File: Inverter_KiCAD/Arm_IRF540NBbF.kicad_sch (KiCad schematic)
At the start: 23 parts, among them Q10 HCPL-315J-500E, Q2 IRF540N, Q3 IRF540N, U1 MPRB2415S-6W, U15 HCPL-7800A, U4 MPRB2415S-6W, U6 GO 10-SME/SP3

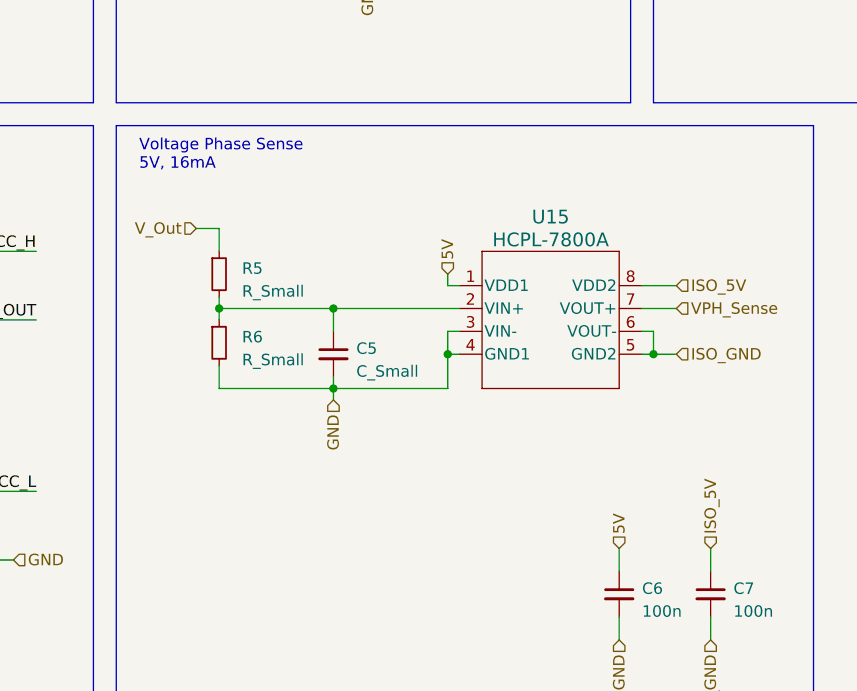
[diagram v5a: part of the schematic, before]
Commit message: start schematic Nucleo board
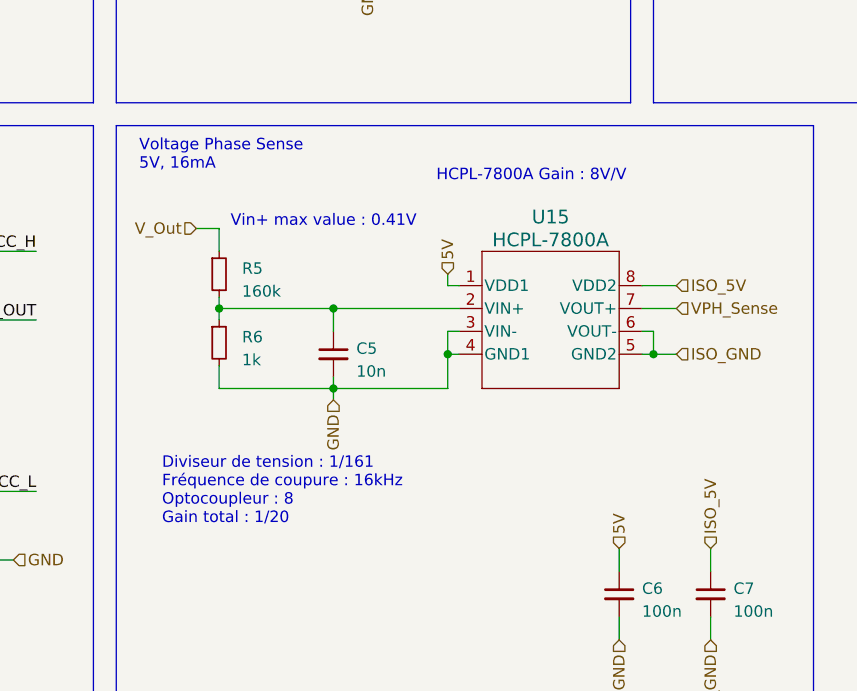
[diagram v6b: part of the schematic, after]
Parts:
- C5: value C_Small -> 10n
- R5: value R_Small -> 160k
- R6: value R_Small -> 1k
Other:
- note added: "Diviseur de tension : 1/161 Fréquence de coupure : 16kHz Optocoupleur : 8 Gain total : 1/20"
- note added: "HCPL-7800A Gain : 8V/V"
- note added: "Vin+ max value : 0.41V"
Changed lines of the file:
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@@
+    (effects (font (size 1.27 1.27)) (justify left bottom))
+  )
+  (text "Vin+ max value : 0.41V" (at 127 96.52 0)
     (effects (font (size 1.27 1.27)) (justify left bottom))
   )
@@
     (effects (font (size 1.27 1.27)) (justify left bottom))
   )
+  (text "Diviseur de tension : 1/161\nFréquence de coupure : 16kHz\nOptocoupleur : 8\nGain total : 1/20"
+    (at 119.38 129.54 0)
+    (effects (font (size 1.27 1.27)) (justify left bottom))
+  )
+  (text "HCPL-7800A Gain : 8V/V" (at 149.86 91.44 0)
+    (effects (font (size 1.27 1.27)) (justify left bottom))
+  )
   (label "Uref" (at 220.98 63.5 0) (fields_autoplaced)
     (effects (font (size 1.27 1.27)) (justify left bottom))
@@
       (effects (font (size 1.27 1.27)) (justify left))
     )
-    (property "Value" "C_Small" (at 140.97 112.4013 0)
+    (property "Value" "10n" (at 140.97 112.4013 0)
       (effects (font (size 1.27 1.27)) (justify left))
     )
@@
       (effects (font (size 1.27 1.27)) (justify left))
     )
-    (property "Value" "R_Small" (at 128.27 111.125 0)
+    (property "Value" "1k" (at 128.27 111.125 0)
       (effects (font (size 1.27 1.27)) (justify left))
     )
@@
       (effects (font (size 1.27 1.27)) (justify left))
     )
-    (property "Value" "R_Small" (at 128.27 103.505 0)
-      (effects (font (size 1.27 1.27)) (justify left))
-    )
+    (property "Value" "160k" (at 128.27 103.505 0)
+      (effects (font (size 1.27 1.27)) (justify left))
+    )

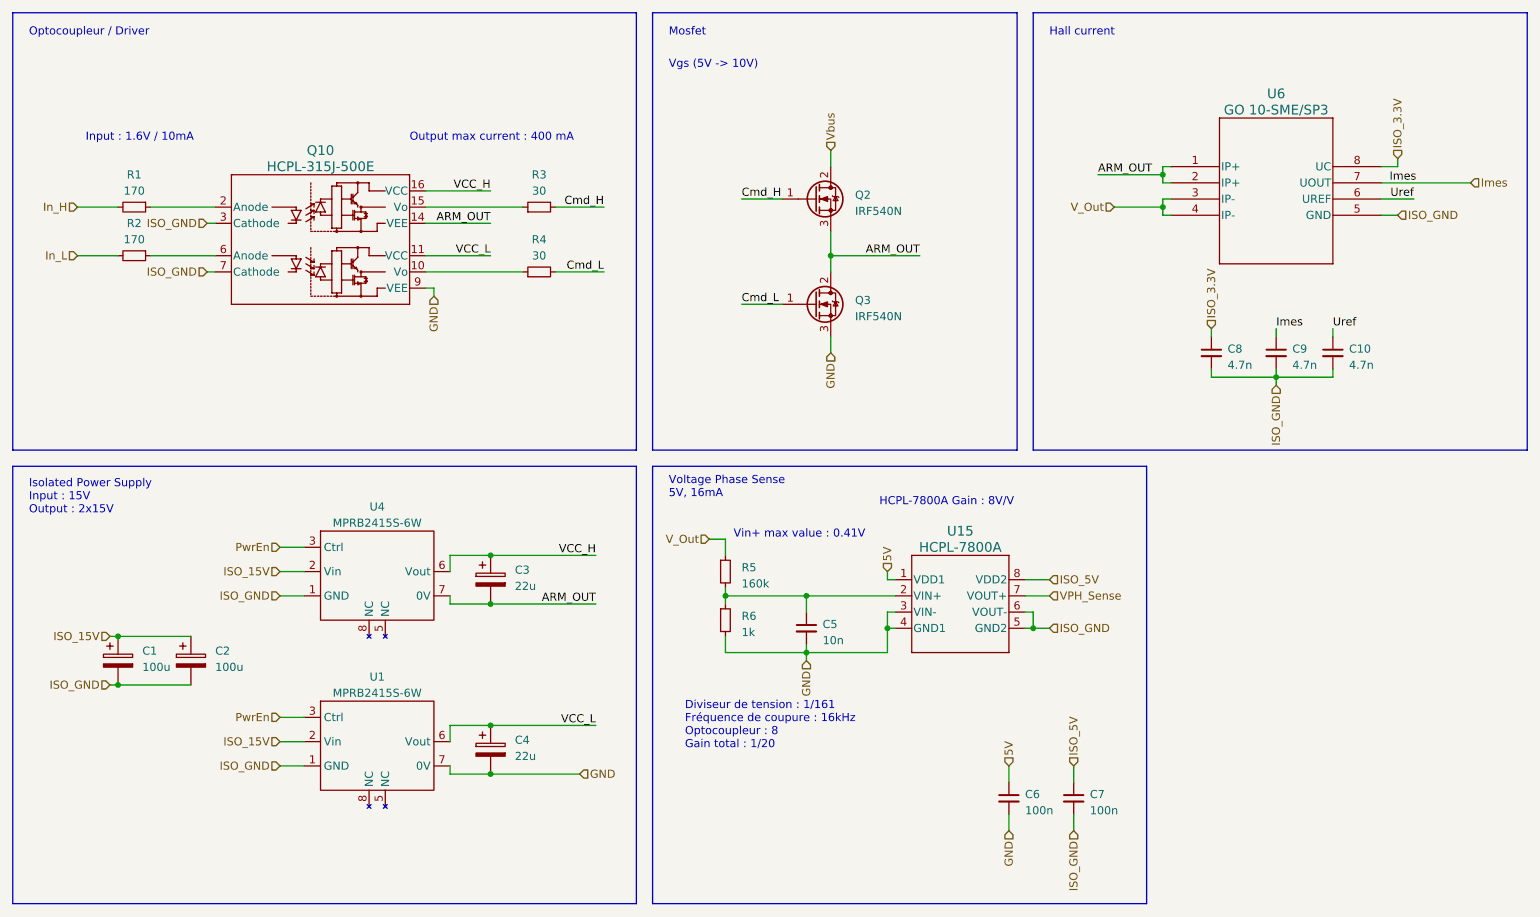
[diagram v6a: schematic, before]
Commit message: clear schematic errors
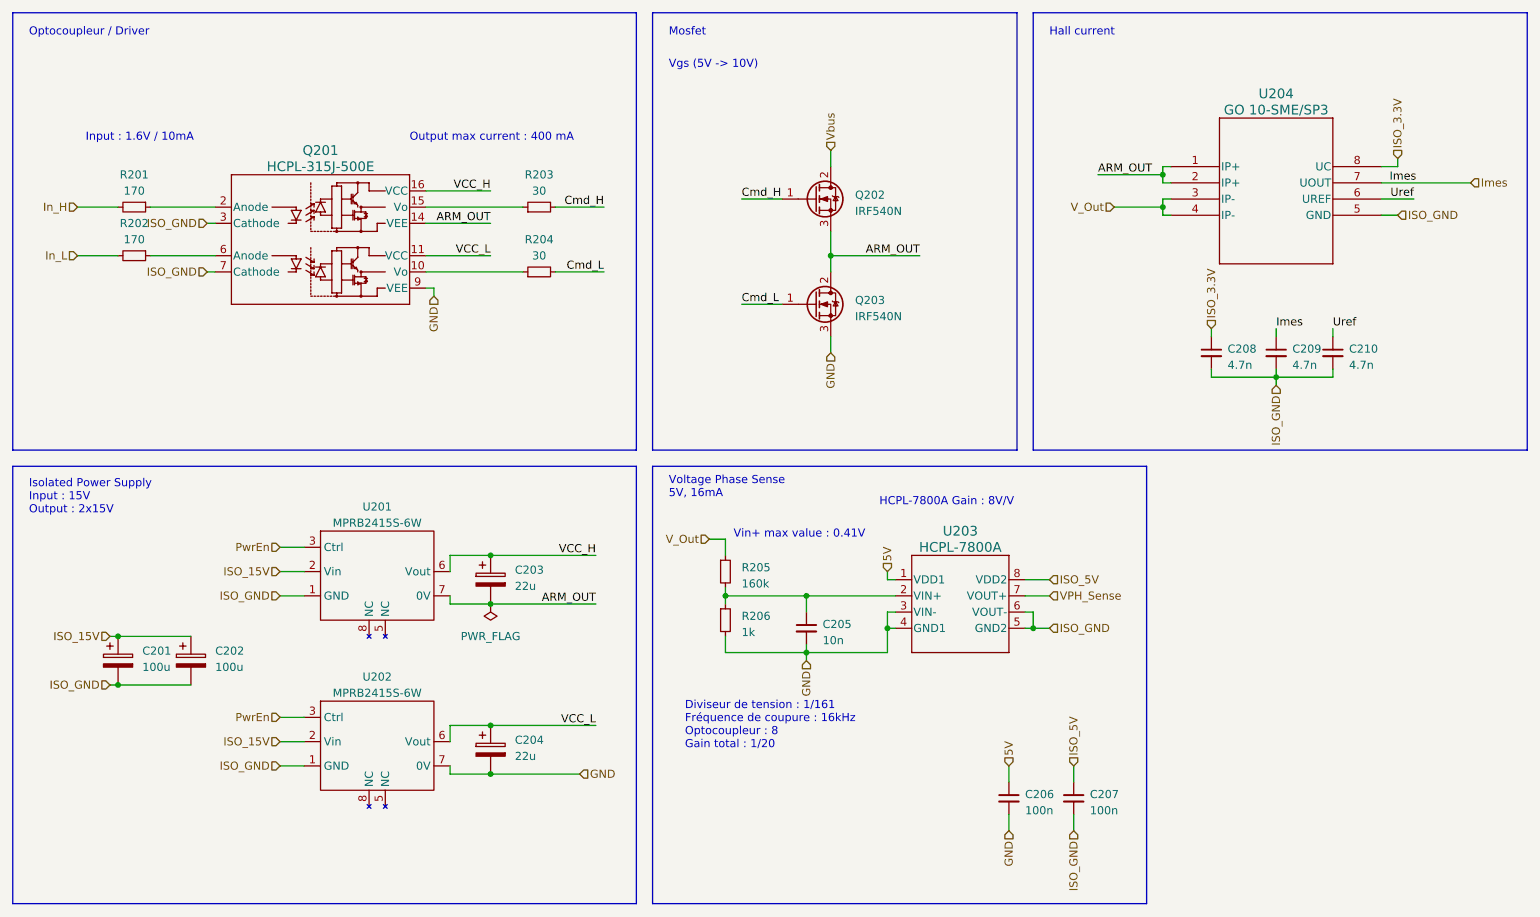
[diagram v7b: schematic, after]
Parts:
- removed U6: GO 10-SME/SP3, Custom:SOIC8-GO-SME&slash_SP3_LEM, symbol Custom:GO_10-SME
- added U204: GO 10-SME/SP3, symbol Custom:GO_10-SME
- U203: renamed from U15; footprint Custom:HCPL-7800A -> (none)
- renumbered C1 to C201, C2 to C202, C3 to C203, C4 to C204, C5 to C205, C6 to C206, C7 to C207, C8 to C208, C9 to C209, C10 to C210, Q10 to Q201, Q2 to Q202, Q3 to Q203, R1 to R201, R2 to R202, R3 to R203, R4 to R204, R5 to R205, R6 to R206, U4 to U201, U1 to U202
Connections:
- net ARM_OUT: now also U204.1 (IP+), U204.2 (IP+)
- net ISO_3.3V: now also U204.8 (UC)
- net ISO_GND: now also U204.5 (GND)
- net Imes: now also U204.7 (UOUT)
- net Uref: now also U204.6 (UREF)
- net V_Out: now also U204.3 (IP-), U204.4 (IP-)

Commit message: end of sch, start pcb
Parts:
- C205: footprint Capacitor_SMD:C_0603_1608Metric_Pad1.08x0.95mm_HandSolder -> Capacitor_SMD:C_0402_1005Metric_Pad0.74x0.62mm_HandSolder
- R201, R202, R205, R206: footprint Resistor_SMD:R_0603_1608Metric_Pad0.98x0.95mm_HandSolder -> Resistor_SMD:R_0402_1005Metric_Pad0.72x0.64mm_HandSolder
- U203: footprint (none) -> Custom:HCPL-7800A
- U204: footprint (none) -> Custom:SOIC8-GO-SME&slash_SP3_LEM
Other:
- company: (none) -> ENSEA
- title: (none) -> AAP Inverter
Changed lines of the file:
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@@
 (kicad_sch (version 20230121) (generator eeschema)
   (paper "A4")
+  (title_block
+    (title "AAP Inverter")
+    (date "2023-05-01")
+    (company "ENSEA")
+  )
   (junction (at 194.31 44.45) (diameter 0) (color 0 0 0 0)
   )
@@
       (effects (font (size 1.27 1.27)))
     )
-    (property "Footprint" "Resistor_SMD:R_0603_1608Metric_Pad0.98x0.95mm_HandSolder" (at 33.02 44.45 0)
+    (property "Footprint" "Resistor_SMD:R_0402_1005Metric_Pad0.72x0.64mm_HandSolder" (at 33.02 44.45 0)
       (effects (font (size 1.27 1.27)) hide)
     )
@@
       (effects (font (size 1.27 1.27)) (justify left))
     )
-    (property "Footprint" "Capacitor_SMD:C_0603_1608Metric_Pad1.08x0.95mm_HandSolder" (at 138.43 110.49 0)
+    (property "Footprint" "Capacitor_SMD:C_0402_1005Metric_Pad0.74x0.62mm_HandSolder" (at 138.43 110.49 0)
       (effects (font (size 1.27 1.27)) hide)
     )
@@
       (effects (font (size 1.27 1.27)))
     )
-    (property "Footprint" "Resistor_SMD:R_0603_1608Metric_Pad0.98x0.95mm_HandSolder" (at 33.02 52.07 0)
+    (property "Footprint" "Resistor_SMD:R_0402_1005Metric_Pad0.72x0.64mm_HandSolder" (at 33.02 52.07 0)
       (effects (font (size 1.27 1.27)) hide)
     )
@@
       (effects (font (size 1.27 1.27)) (justify left))
     )
-    (property "Footprint" "Resistor_SMD:R_0603_1608Metric_Pad0.98x0.95mm_HandSolder" (at 125.73 109.22 0)
+    (property "Footprint" "Resistor_SMD:R_0402_1005Metric_Pad0.72x0.64mm_HandSolder" (at 125.73 109.22 0)
       (effects (font (size 1.27 1.27)) hide)
     )
@@
       (effects (font (size 1.27 1.27)) (justify left))
     )
-    (property "Footprint" "Resistor_SMD:R_0603_1608Metric_Pad0.98x0.95mm_HandSolder" (at 125.73 101.6 0)
+    (property "Footprint" "Resistor_SMD:R_0402_1005Metric_Pad0.72x0.64mm_HandSolder" (at 125.73 101.6 0)
       (effects (font (size 1.27 1.27)) hide)
     )
@@
       (effects (font (size 1.524 1.524)))
     )
-    (property "Footprint" "" (at 166.37 121.92 0)
+    (property "Footprint" "Custom:HCPL-7800A" (at 166.37 121.92 0)
       (effects (font (size 1.27 1.27) italic) hide)
     )
@@
       (effects (font (size 1.524 1.524)))
     )
-    (property "Footprint" "" (at 213.36 21.59 0)
+    (property "Footprint" "Custom:SOIC8-GO-SME&slash_SP3_LEM" (at 213.36 21.59 0)
       (effects (font (size 1.27 1.27) italic) hide)
     )
